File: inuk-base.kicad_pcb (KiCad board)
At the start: 2 copper layers, 100 x 80 mm, 82 parts, among them J1 Conn_02x05_Odd_Even, J2 Conn_01x06, J3 Conn_01x02_Male, J4 Conn_01x02_Male, J5 Conn_01x08, J6 Conn_01x03_Male, J7 Conn_01x03_Male, J8 Conn_01x02_Male, Q1 DMG3406L, Q2 DMG3406L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

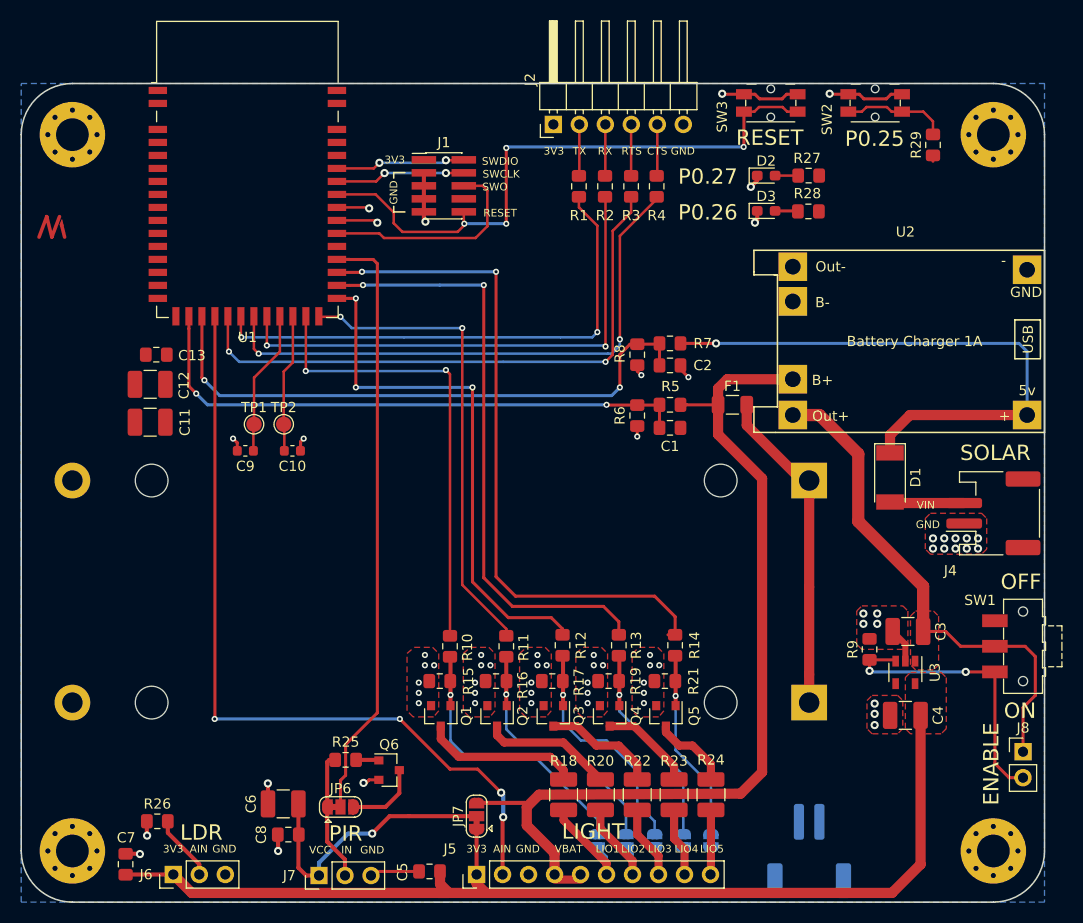
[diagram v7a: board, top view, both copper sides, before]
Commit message: changed pcb size to 100 x 70 and made progress on layout
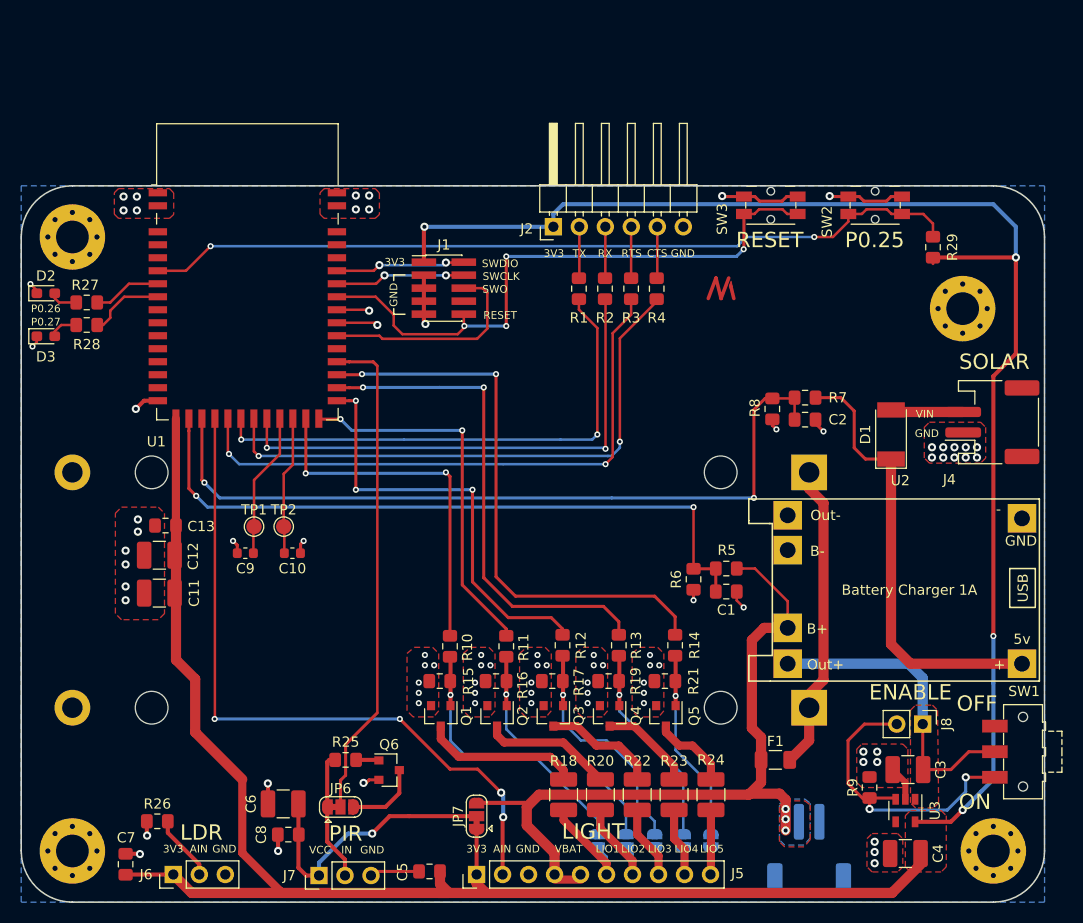
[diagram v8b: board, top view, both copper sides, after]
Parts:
- moved R27 71.6 mm to (61.4, 86.4)
- moved D3 71.5 mm to (57.4, 89.7)
- moved R28 71.4 mm to (61.4, 88.6)
- moved D2 71.3 mm to (57.4, 85.5)
- moved U4 65.7 mm to (123.4, 85.0)
- moved F1 35.0 mm to (128.7, 131.1)
- moved U2 24.3 mm to (154.5, 123.4)
- moved H3 17.3 mm to (147.0, 87.0)
- moved C1 16.9 mm to (123.9, 114.7)
- moved R5 16.9 mm to (123.9, 112.4)
- moved R6 16.9 mm to (120.7, 113.5)
- moved C11 16.7 mm to (68.5, 114.8)
- moved C13 16.7 mm to (69.1, 108.2)
- moved C12 16.7 mm to (68.5, 111.1)
- moved R8 14.2 mm to (128.4, 96.8)
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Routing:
- net +3V3: track 104.9 -> 277.1 mm, vias 0 -> 4
- net /cpu/P0.25: track 10.9 -> 81.1 mm, vias 0 -> 2
- net /power/VIN: track 49.7 -> 30.5 mm
- net /power/VSOLAR_ADC: track 57.6 -> 75.9 mm
- net +BATT: track 91.0 -> 73.8 mm, vias 0 -> 3
- net /power/VSOLAR: track 56.4 -> 43.7 mm, vias 1 -> 0
- net /power/VBAT_ADC: track 55.8 -> 67.4 mm
- net /cpu/lio5: track 67.0 -> 56.3 mm
- net /cpu/pir_input: track 58.7 -> 48.7 mm
- net /cpu/lio4: track 59.2 -> 49.2 mm
- net /cpu/lio3: track 52.2 -> 42.2 mm
- net /cpu/lio2: track 46.3 -> 36.3 mm
- net /cpu/lio1: track 45.2 -> 35.2 mm
- net /cpu/ain2: track 78.5 -> 68.5 mm
- net /cpu/P0.27: track 0.00 -> 7.48 mm
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- added copper zone on B.Cu, net +BATT
- added copper zone on F.Cu, net +BATT
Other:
- board size 100 x 80 mm -> 100 x 70 mm
